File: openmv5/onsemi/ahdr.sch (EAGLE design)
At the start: 75 parts, among them IC1 AR0231AT7C00XUEA0-DRBR-E, IC2 TLV62568PDDCR, IC3 MIC5365-2.8YC5-TR, J1 DF12-36-DP, Q1 PMXB120EPEZ

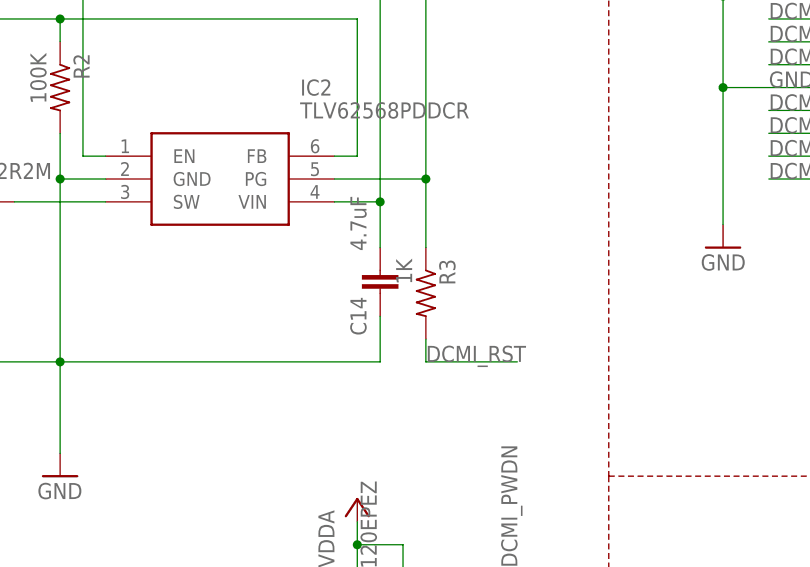
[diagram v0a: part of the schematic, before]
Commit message: Update resistor value
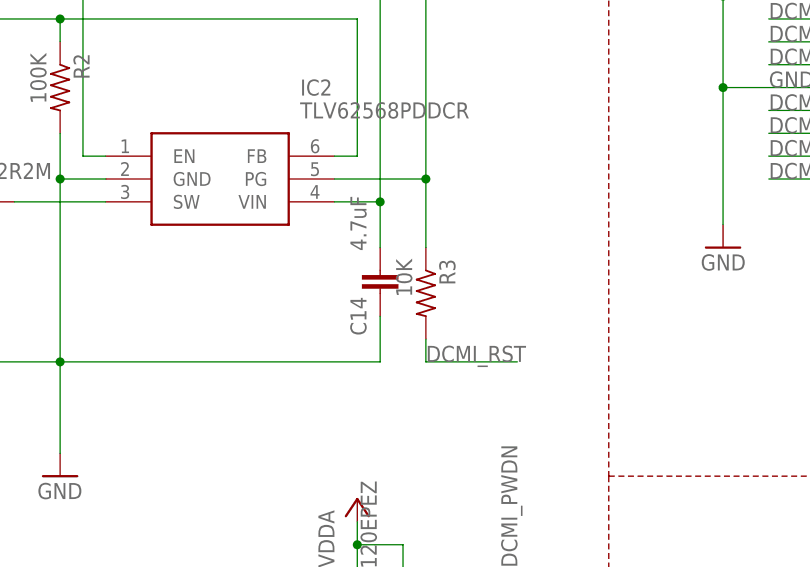
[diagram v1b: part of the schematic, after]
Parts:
- R3: value 1K -> 10K; MPN CRCW04021K00FKEDC -> AC0402FR-1310KL
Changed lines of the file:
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@@
 <attribute name="MPN" value="MFBM1V1005-101-R"/>
 </part>
-<part name="R3" library="rcl" library_urn="urn:adsk.eagle:library:334" deviceset="R-US_" device="R0402" package3d_urn="urn:adsk.eagle:package:23547/3" value="1K">
+<part name="R3" library="rcl" library_urn="urn:adsk.eagle:library:334" deviceset="R-US_" device="R0402" package3d_urn="urn:adsk.eagle:package:23547/3" value="10K">
 <spice>
 <pinmapping spiceprefix="R">
@@
 </pinmapping>
 </spice>
-<attribute name="MPN" value="CRCW04021K00FKEDC"/>
+<attribute name="MPN" value="AC0402FR-1310KL"/>
 </part>
 </parts>
